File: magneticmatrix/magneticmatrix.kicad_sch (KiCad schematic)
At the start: 9 parts, among them Q1 2N7000, SW1 SW_SPST, U1 DRV5055A1xDBZxQ1, U2 MAX603

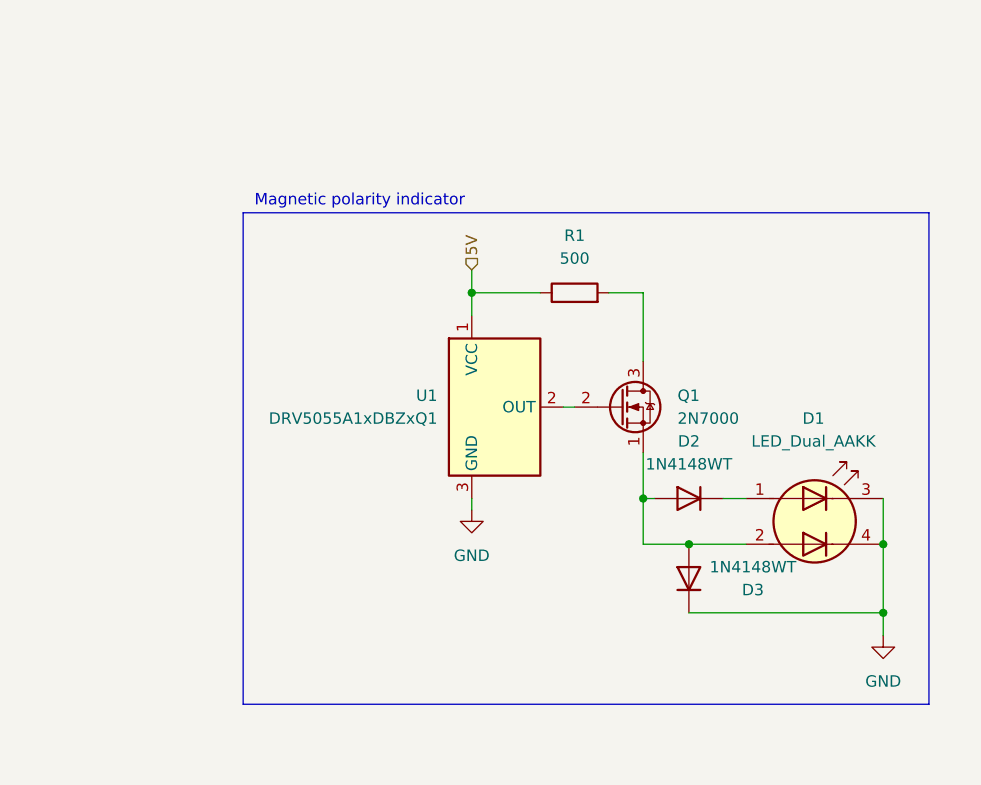
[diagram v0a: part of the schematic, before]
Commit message: RGB instead of bicolor
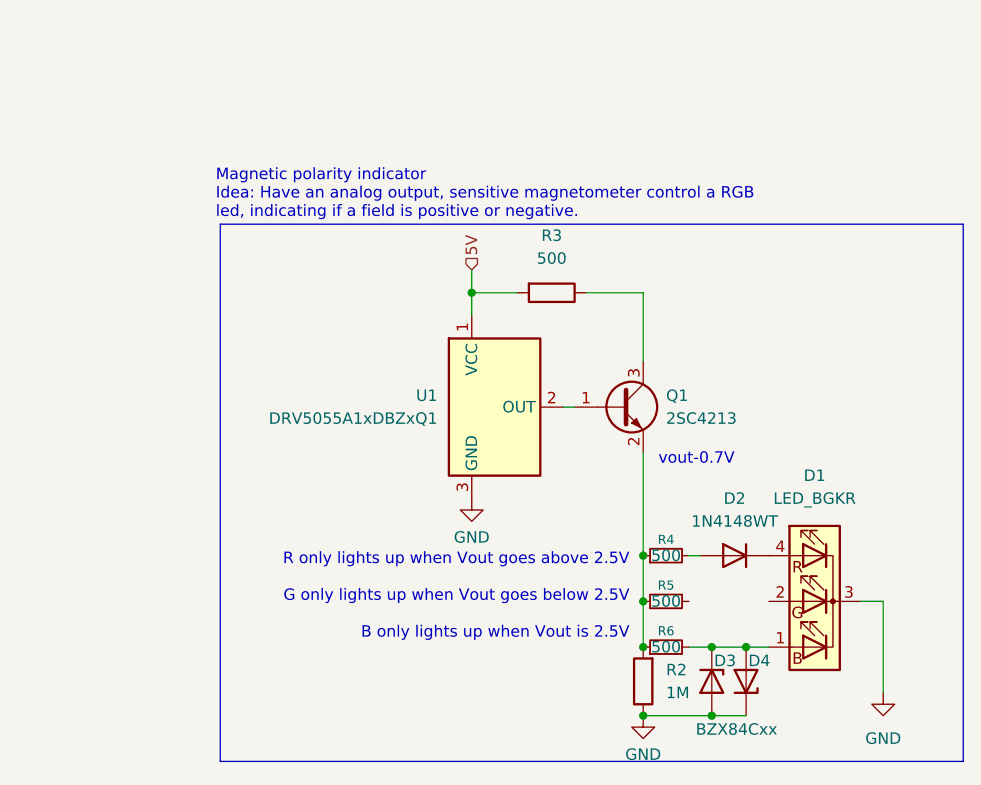
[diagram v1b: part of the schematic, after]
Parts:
- removed D1: LED_Dual_AAKK, LED_SMD:LED_LiteOn_LTST-C19HE1WT, symbol Device:LED_Dual_AAKK
- removed D3: 1N4148WT, Diode_THT:D_DO-35_SOD27_P2.54mm_Vertical_AnodeUp, symbol Diode:1N4148WT
- removed Q1: 2N7000, Package_TO_SOT_THT:TO-92_Inline, symbol Transistor_FET:2N7000
- removed R1: 500, Resistor_SMD:R_01005_0402Metric, symbol Device:R
- added D1: LED_BGKR, LED_SMD:LED_ASMB-KTF0-0A306, symbol Device:LED_BGKR
- added D3, D4: BZX84Cxx, Package_TO_SOT_SMD:SOT-23, symbol Diode:BZX84Cxx
- added Q1: 2SC4213, Package_TO_SOT_SMD:SOT-323_SC-70, symbol Transistor_BJT:2SC4213
- added R2: 1M, Resistor_SMD:R_01005_0402Metric, symbol Device:R
- added R3: 500, Resistor_SMD:R_01005_0402Metric, symbol Device:R
- added R4, R5, R6: 500, symbol Device:R_Small
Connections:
- net 5V: now also R3.2
- net GND: now also D1.3 (K), D3.1 (A), D4.3 (K), R2.1
- net at D2.2 (A): now also R4.2
- net at U1.2 (OUT): now also Q1.1 (B)
- net at D2.1 (K): now also D1.4 (RA)
- new net: D1.1 (BA), D3.3 (K), D4.1 (A), R6.2
- new net: Q1.3 (C), R3.1
- new net: Q1.2 (E), R2.2, R4.1, R5.1, R6.1
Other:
- note added: "Magnetic polarity indicator Idea: Have an analog output, sensitive magnetometer control a RGB led, indicating if a field is positive or negative."
- note added: "R only lights up when Vout goes above 2.5V G only lights up when Vout goes below 2.5V B only lights up when Vout is 2.5V"
- note added: "vout-0.7V"
- note removed: "Magnetic polarity indicator"
- moved on the sheet: D2

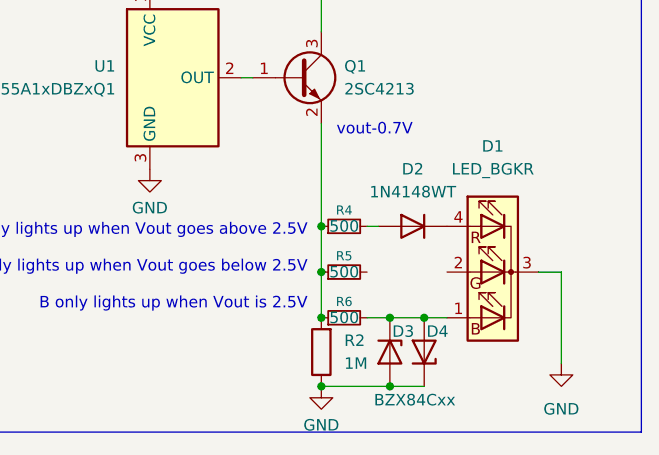
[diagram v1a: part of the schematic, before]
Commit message: RGB instead of bicolor
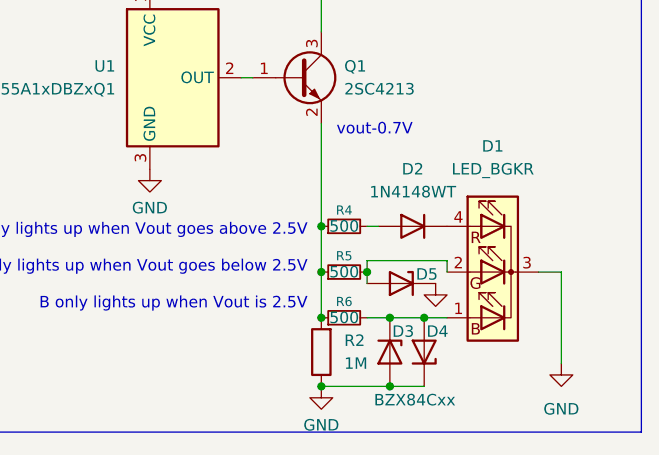
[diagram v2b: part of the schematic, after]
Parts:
- added D5: BZX84Cxx, Package_TO_SOT_SMD:SOT-23, symbol Diode:BZX84Cxx
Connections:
- net GND: now also D5.3 (K)
- net at D1.2 (GA): now also R5.2, D5.1 (A)
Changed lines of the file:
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@@
 		(color 0 0 0 0)
 	)
+	(junction
+		(at 165.1 86.36)
+		(diameter 0)
+		(color 0 0 0 0)
+	)
 	(wire
 		(pts
@@
 	(wire
 		(pts
+			(xy 165.1 85.09) (xy 173.99 85.09)
+		)
+		(stroke
+			(width 0)
+			(type default)
+		)
+	)
+	(wire
+		(pts
 			(xy 68.58 33.02) (xy 71.12 33.02)
 		)
@@
 	(wire
 		(pts
+			(xy 165.1 85.09) (xy 165.1 86.36)
+		)
+		(stroke
+			(width 0)
+			(type default)
+		)
+	)
+	(wire
+		(pts
+			(xy 165.1 86.36) (xy 165.1 87.63)
+		)
+		(stroke
+			(width 0)
+			(type default)
+		)
+	)
+	(wire
+		(pts
 			(xy 167.64 99.06) (xy 171.45 99.06)
 		)
@@
 		(pts
 			(xy 29.21 33.02) (xy 31.75 33.02)
+		)
+		(stroke
+			(width 0)
+			(type default)
+		)
+	)
+	(wire
+		(pts
+			(xy 173.99 85.09) (xy 173.99 86.36)
 		)
 		(stroke
@@
 	)
 	(symbol
+		(lib_id "power:GND")
+		(at 172.72 87.63 0)
+		(unit 1)
+		(exclude_from_sim no)
+		(in_bom yes)
+		(on_board yes)
+		(dnp no)
+		(property "Reference" "#PWR06"
+			(at 172.72 93.98 0)
+			(effects
+				(font
+					(size 1.27 1.27)
+				)
+				(hide yes)
+			)
+		)
+		(property "Value" "GND"
+			(at 172.72 91.948 0)
+			(effects
+				(font
+					(size 1.27 1.27)
+				)
+				(hide yes)
+			)
+		)
+		(property "Footprint" ""
+			(at 172.72 87.63 0)
+			(effects
+				(font
+					(size 1.27 1.27)
+				)
+				(hide yes)
+			)
+		)
+		(property "Datasheet" ""
+			(at 172.72 87.63 0)
+			(effects
+				(font
+					(size 1.27 1.27)
+				)
+				(hide yes)
+			)
+		)
+		(property "Description" "Power symbol creates a global label with name \"GND\" , ground"
+			(at 172.72 87.63 0)
+			(effects
+				(font
+					(size 1.27 1.27)
+				)
+				(hide yes)
+			)
+		)
+		(pin "1"
+		)
+		(instances
+			(project "magneticmatrix"
+				(path "/860504d8-3138-468b-8439-ff428c9ca2aa"
+					(reference "#PWR06")
+					(unit 1)
+				)
+			)
+		)
+	)
+	(symbol
 		(lib_id "Device:R")
 		(at 160.02 95.25 180)
@@
 					(unit 1)
 				)
+			)
+		)
+	)
+	(symbol
+		(lib_id "Diode:BZX84Cxx")
+		(at 168.91 87.63 0)
+		(mirror y)
+		(unit 1)
+		(exclude_from_sim no)
+		(in_bom yes)
+		(on_board yes)
+		(dnp no)
+		(property "Reference" "D5"
+			(at 172.974 86.614 0)
+			(effects
+				(font
+					(size 1.27 1.27)
+				)
+				(justify left)
+			)
+		)
+		(property "Value" "BZX84Cxx"
+			(at 174.244 93.218 90)
+			(effects
+				(font
+					(size 1.27 1.27)
+				)
+				(justify left)
+				(hide yes)
+			)
+		)
+		(property "Footprint" "Package_TO_SOT_SMD:SOT-23"
+			(at 168.91 87.63 0)
+			(effects
+				(font
+					(size 1.27 1.27)
+				)
+				(hide yes)
+			)
+		)
+		(property "Datasheet" "https://diotec.com/tl_files/diotec/files/pdf/datasheets/bzx84c2v4.pdf"
+			(at 168.91 87.63 0)
+			(effects
+				(font
+					(size 1.27 1.27)
+				)
+				(hide yes)
+			)
+		)
+		(property "Description" "300mW Zener Diode, SOT-23"
+			(at 168.91 87.63 0)
+			(effects
+				(font
+					(size 1.27 1.27)
+				)
+				(hide yes)
+			)
+		)
+		(pin "2"
+		)
+		(pin "3"
+		)
+		(pin "1"
+		)
+		(instances
+			(project "magneticmatrix"
+				(path "/860504d8-3138-468b-8439-ff428c9ca2aa"
+					(reference "D5")
+					(unit 1)
+				)

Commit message: added opamp version
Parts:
- added C1: C, symbol Device:C
- added C2: 1u, symbol Device:C
- added D6: LED_BGKR, LED_SMD:LED_ASMB-KTF0-0A306, symbol Device:LED_BGKR
- added D7: BZX84Cxx, Package_TO_SOT_SMD:SOT-23, symbol Diode:BZX84Cxx
- added R1: 500, Resistor_SMD:R_01005_0402Metric, symbol Device:R
- added U4: DRV5055A1xDBZxQ1, Package_TO_SOT_SMD:SOT-23, symbol Sensor_Magnetic:DRV5055A1xDBZxQ1
- added U5: TL082, Package_SO:TSSOP-8_3x3mm_P0.65mm, symbol Amplifier_Operational:TL082
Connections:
- net 5V: now also R1.1, U4.1 (VCC), U5.8 (V+)
- net GND: now also D6.3 (K), D7.1 (A), U4.3 (GND), U5.4 (V-)
- new net: C1.1, C2.1, D6.1 (BA)
- new net: C1.2, D6.2 (GA), U5.7
- new net: U4.2 (OUT), U5.3 (+), U5.6 (-)
- new net: C2.2, D6.4 (RA), U5.1
- new net Vmid: D7.3 (K), R1.2, U5.2 (-), U5.5 (+)
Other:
- note added: "caps to have B also activate when state is switched so there is a small gradient effect. it's there, might as well use it"
- note added: "easierBOM version"

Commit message: added some pcb stuff
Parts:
- C1: value C -> 1u; footprint (none) -> Capacitor_SMD:C_01005_0402Metric_Pad0.57x0.30mm_HandSolder
- C2: footprint (none) -> Capacitor_SMD:C_01005_0402Metric_Pad0.57x0.30mm_HandSolder
- D1, D2, D3, D4, D5, Q1, R2, R3, R4, R5, R6, U1: now left out of the parts list
